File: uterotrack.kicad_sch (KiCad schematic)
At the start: 77 parts, among them J1 RFShield, J2 MicroSD_Card, J3 Argos_Prog, J4 AS5510, J5 Prog, J6 EXP, Q1 DMP2110UW, Q10 MMBT2222, Q11 MMBT2222, Q12 MMBT2222, Q13 MMBT2222, Q2 DMP2110UW, Q3 MMBT2222, Q4 DMP2110UW, Q5 DMP2110UW, Q6 MMBT2222, Q7 SiS415DNT, Q8 DMP2110UW, Q9 MMBT2222, U1 Argos_SMD, U2 ESP32-S3-WROOM-1, U3 keller_6LHPD, U4 RV-3032-C7, U5 CAM-M8Q

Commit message: Change manf# and footprint of resistor of 4k7, 20k and 100k to 0402
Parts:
- J3: manf# (none) -> 53047-0510
- R15, R16, R17, R23, R24, R26, R27, R28, R30, R31, R32, R33, R34, R36, R37: footprint Resistor_SMD:R_0603_1608Metric -> Resistor_SMD:R_0402_1005Metric; manf# CRCW0603100KFKEAC -> CRCW0402100KFKEDC
- R19, R20, R21, R22, R25: footprint Resistor_SMD:R_0603_1608Metric -> Resistor_SMD:R_0402_1005Metric; manf# CRCW06034K70FKEAC -> CRCW04024K70FKEDC
- R29, R35: footprint Resistor_SMD:R_0603_1608Metric -> Resistor_SMD:R_0402_1005Metric; manf# CRCW060320K0FKEAC -> CRCW040220K0FKEDC
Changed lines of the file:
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@@
 			)
 		)
-		(property "Footprint" "Resistor_SMD:R_0603_1608Metric"
+		(property "Footprint" "Resistor_SMD:R_0402_1005Metric"
 			(at 64.77 248.158 90)
 			(effects
@@
 			)
 		)
-		(property "manf#" "CRCW0603100KFKEAC"
+		(property "manf#" "CRCW0402100KFKEDC"
 			(at 64.77 246.38 0)
 			(effects
@@
 			)
 		)
-		(property "Footprint" "Resistor_SMD:R_0603_1608Metric"
+		(property "Footprint" "Resistor_SMD:R_0402_1005Metric"
 			(at 87.63 169.418 90)
 			(effects
@@
 			)
 		)
-		(property "manf#" "CRCW0603100KFKEAC"
+		(property "manf#" "CRCW0402100KFKEDC"
 			(at 87.63 167.64 0)
 			(effects
@@
 			)
 		)
-		(property "Footprint" "Resistor_SMD:R_0603_1608Metric"
+		(property "Footprint" "Resistor_SMD:R_0402_1005Metric"
 			(at 82.042 156.21 90)
 			(effects
@@
 			)
 		)
-		(property "manf#" "CRCW0603100KFKEAC"
+		(property "manf#" "CRCW0402100KFKEDC"
 			(at 83.82 156.21 0)
 			(effects
@@
 			)
 		)
-		(property "Footprint" "Resistor_SMD:R_0603_1608Metric"
+		(property "Footprint" "Resistor_SMD:R_0402_1005Metric"
 			(at 120.142 234.95 90)
 			(effects
@@
 			)
 		)
-		(property "manf#" "CRCW0603100KFKEAC"
+		(property "manf#" "CRCW0402100KFKEDC"
 			(at 121.92 234.95 0)
 			(effects
@@
 			)
 		)
-		(property "Footprint" "Resistor_SMD:R_0603_1608Metric"
+		(property "Footprint" "Resistor_SMD:R_0402_1005Metric"
 			(at 62.23 155.702 90)
 			(effects
@@
 			)
 		)
-		(property "manf#" "CRCW06034K70FKEAC"
+		(property "manf#" "CRCW04024K70FKEDC"
 			(at 62.23 157.48 0)
 			(effects
@@
 			)
 		)
-		(property "Footprint" "Resistor_SMD:R_0603_1608Metric"
+		(property "Footprint" "Resistor_SMD:R_0402_1005Metric"
 			(at 108.458 247.65 90)
 			(effects
@@
 			)
 		)
-		(property "manf#" "CRCW060320K0FKEAC"
+		(property "manf#" "CRCW040220K0FKEDC"
 			(at 106.68 247.65 0)
 			(effects
@@
 			)
 		)
-		(property "Footprint" "Resistor_SMD:R_0603_1608Metric"
+		(property "Footprint" "Resistor_SMD:R_0402_1005Metric"
 			(at 92.202 173.99 90)
 			(effects
@@
 			)
 		)
-		(property "manf#" "CRCW0603100KFKEAC"
+		(property "manf#" "CRCW0402100KFKEDC"
 			(at 93.98 173.99 0)
 			(effects
@@
 			)
 		)
-		(property "Footprint" "Resistor_SMD:R_0603_1608Metric"
+		(property "Footprint" "Resistor_SMD:R_0402_1005Metric"
 			(at 62.23 156.718 90)
 			(effects
@@
 			)
 		)
-		(property "manf#" "CRCW06034K70FKEAC"
+		(property "manf#" "CRCW04024K70FKEDC"
 			(at 62.23 154.94 0)
 			(effects
@@
 			)
 		)
-		(property "Footprint" "Resistor_SMD:R_0603_1608Metric"
+		(property "Footprint" "Resistor_SMD:R_0402_1005Metric"
 			(at 59.182 234.95 90)
 			(effects
@@
 			)
 		)
-		(property "manf#" "CRCW0603100KFKEAC"
+		(property "manf#" "CRCW0402100KFKEDC"
 			(at 60.96 234.95 0)
 			(effects
@@
 			)
 		)
-		(property "Footprint" "Resistor_SMD:R_0603_1608Metric"
+		(property "Footprint" "Resistor_SMD:R_0402_1005Metric"
 			(at 196.85 260.858 90)
 			(effects
@@
 			)
 		)
-		(property "manf#" "CRCW0603100KFKEAC"
+		(property "manf#" "CRCW0402100KFKEDC"
 			(at 196.85 259.08 0)
 			(effects
@@
 			)
 		)
-		(property "Footprint" "Resistor_SMD:R_0603_1608Metric"
+		(property "Footprint" "Resistor_SMD:R_0402_1005Metric"
 			(at 125.73 248.158 90)
 			(effects
@@
 			)
 		)
-		(property "manf#" "CRCW0603100KFKEAC"
+		(property "manf#" "CRCW0402100KFKEDC"
 			(at 125.73 246.38 0)
 			(effects
@@
 			)
 		)
-		(property "Footprint" "Resistor_SMD:R_0603_1608Metric"
+		(property "Footprint" "Resistor_SMD:R_0402_1005Metric"
 			(at 290.83 85.598 90)
 			(effects
@@
 			)
 		)
-		(property "manf#" "CRCW0603100KFKEAC"
+		(property "manf#" "CRCW0402100KFKEDC"
 			(at 290.83 83.82 0)
 			(effects
@@
 			)
 		)
-		(property "Footprint" "Resistor_SMD:R_0603_1608Metric"
+		(property "Footprint" "Resistor_SMD:R_0402_1005Metric"
 			(at 105.41 113.538 90)
 			(effects
@@
 			)
 		)
-		(property "manf#" "CRCW06034K70FKEAC"
+		(property "manf#" "CRCW04024K70FKEDC"
 			(at 105.41 111.76 0)
 			(effects
@@
 			)
 		)
+		(property "manf#" "53047-0510"
+			(at 287.02 114.3 0)
+			(effects
+				(font
+					(size 1.27 1.27)
+				)
+				(hide yes)
+			)
+		)
 		(pin "2"
 		)
@@
 			)
 		)
-		(property "Footprint" "Resistor_SMD:R_0603_1608Metric"
+		(property "Footprint" "Resistor_SMD:R_0402_1005Metric"
 			(at 296.418 72.39 90)
 			(effects
@@
 			)
 		)
-		(property "manf#" "CRCW0603100KFKEAC"
+		(property "manf#" "CRCW0402100KFKEDC"
 			(at 294.64 72.39 0)
 			(effects
@@
 			)
 		)
-		(property "Footprint" "Resistor_SMD:R_0603_1608Metric"
+		(property "Footprint" "Resistor_SMD:R_0402_1005Metric"
 			(at 127.762 156.21 90)
 			(effects
@@
 			)
 		)
-		(property "manf#" "CRCW0603100KFKEAC"
+		(property "manf#" "CRCW0402100KFKEDC"
 			(at 129.54 156.21 0)
 			(effects
@@
 			)
 		)
-		(property "Footprint" "Resistor_SMD:R_0603_1608Metric"
+		(property "Footprint" "Resistor_SMD:R_0402_1005Metric"
 			(at 46.482 74.93 90)
 			(effects
@@
 			)
 		)
-		(property "manf#" "CRCW0603100KFKEAC"
+		(property "manf#" "CRCW0402100KFKEDC"
 			(at 48.26 74.93 0)
 			(effects
@@
 			)
 		)
-		(property "Footprint" "Resistor_SMD:R_0603_1608Metric"
+		(property "Footprint" "Resistor_SMD:R_0402_1005Metric"
 			(at 69.342 252.73 90)
 			(effects
@@
 			)
 		)
-		(property "manf#" "CRCW0603100KFKEAC"
+		(property "manf#" "CRCW0402100KFKEDC"
 			(at 71.12 252.73 0)
 			(effects
@@
 			)
 		)
-		(property "Footprint" "Resistor_SMD:R_0603_1608Metric"
+		(property "Footprint" "Resistor_SMD:R_0402_1005Metric"
 			(at 49.53 109.982 90)
 			(effects
@@
 			)
 		)
-		(property "manf#" "CRCW06034K70FKEAC"
+		(property "manf#" "CRCW04024K70FKEDC"
 			(at 49.53 111.76 0)
 			(effects
@@
 			)
 		)
-		(property "Footprint" "Resistor_SMD:R_0603_1608Metric"
+		(property "Footprint" "Resistor_SMD:R_0402_1005Metric"
 			(at 201.93 245.618 90)
 			(effects
@@
 			)
 		)
-		(property "manf#" "CRCW0603100KFKEAC"
+		(property "manf#" "CRCW0402100KFKEDC"
 			(at 201.93 243.84 0)
 			(effects
@@
 			)
 		)
-		(property "Footprint" "Resistor_SMD:R_0603_1608Metric"
+		(property "Footprint" "Resistor_SMD:R_0402_1005Metric"
 			(at 108.458 234.95 90)
 			(effects
@@
 			)
 		)
-		(property "manf#" "CRCW060320K0FKEAC"
+		(property "manf#" "CRCW040220K0FKEDC"
 			(at 106.68 234.95 0)
 			(effects
@@
 			)
 		)
-		(property "Footprint" "Resistor_SMD:R_0603_1608Metric"
+		(property "Footprint" "Resistor_SMD:R_0402_1005Metric"
 			(at 49.53 110.998 90)
 			(effects
@@
 			)
 		)
-		(property "manf#" "CRCW06034K70FKEAC"
+		(property "manf#" "CRCW04024K70FKEDC"
 			(at 49.53 109.22 0)
 			(effects
@@
 			)
 		)
-		(property "Footprint" "Resistor_SMD:R_0603_1608Metric"
+		(property "Footprint" "Resistor_SMD:R_0402_1005Metric"
 			(at 161.29 245.618 90)
 			(effects
@@
 			)
 		)
-		(property "manf#" "CRCW0603100KFKEAC"
+		(property "manf#" "CRCW0402100KFKEDC"
 			(at 161.29 243.84 0)
 			(effects

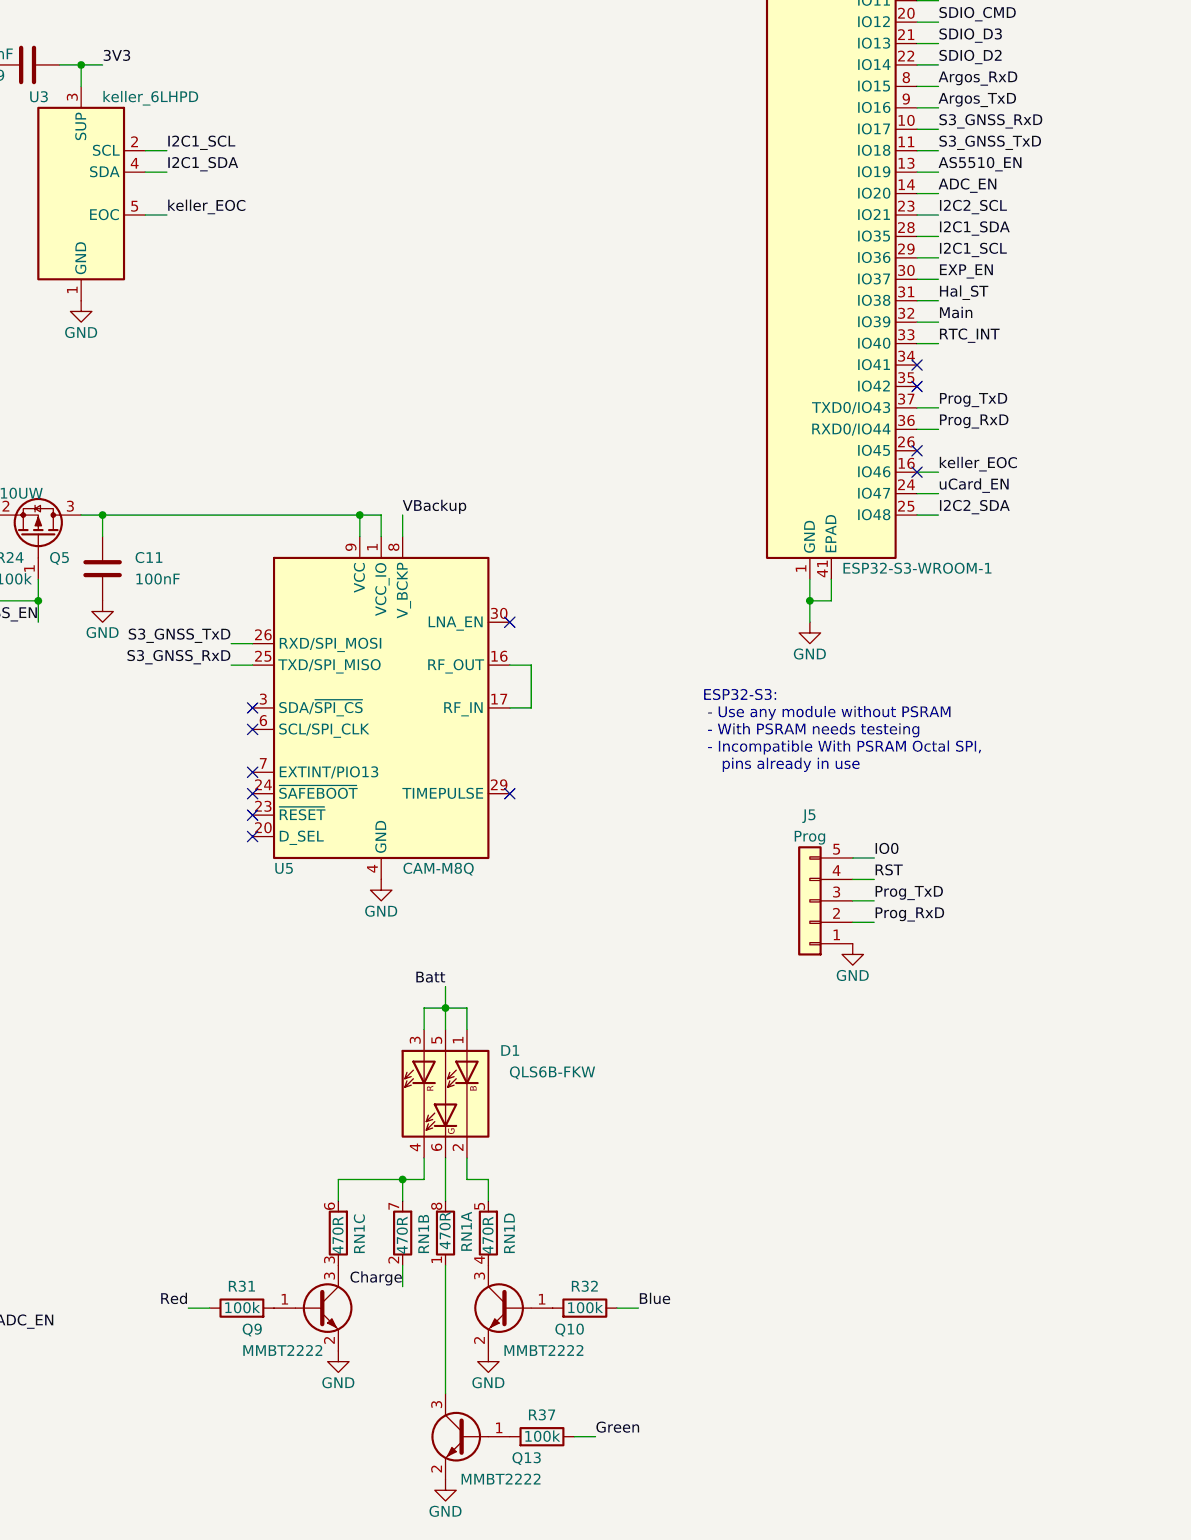
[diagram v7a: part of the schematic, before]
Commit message: Move AS5510_EN to IO42 and switch led red with charge in RN1
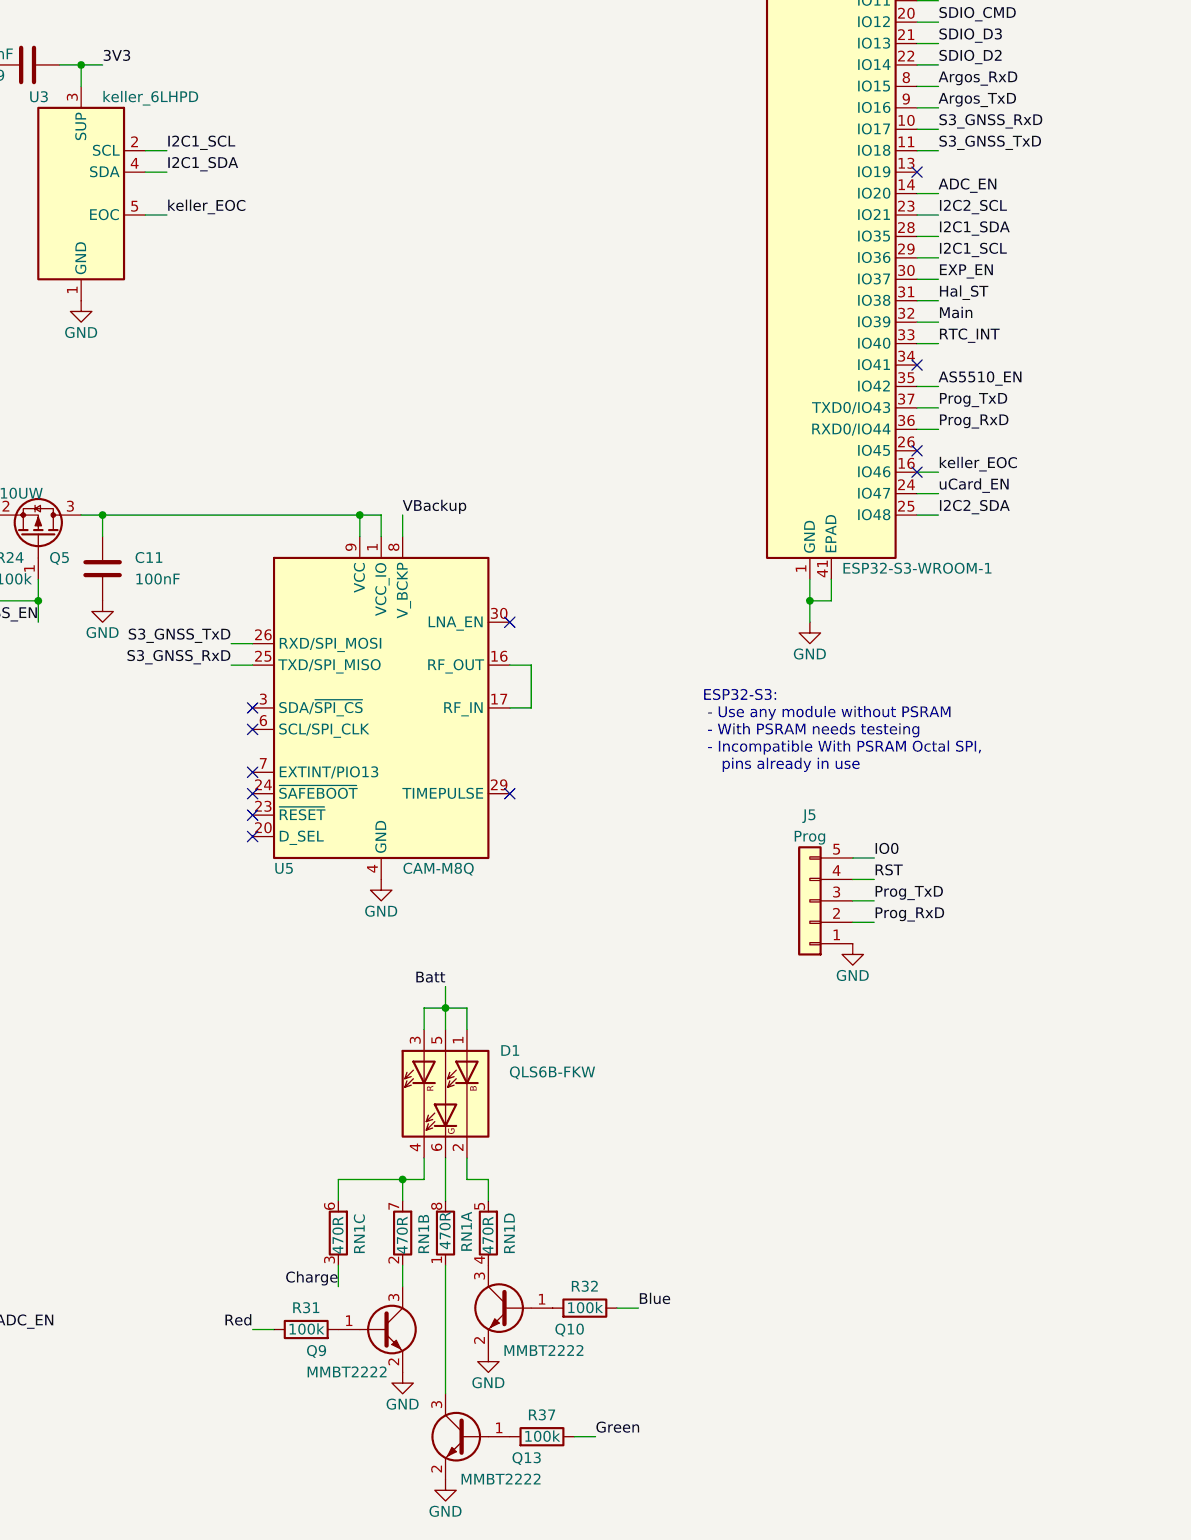
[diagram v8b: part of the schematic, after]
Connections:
- net AS5510_EN: now also U2.35 (IO42); no longer U2.13 (IO19)
- net Charge: now also RN1.3 (R3.1); no longer RN1.2 (R2.1)
- net at Q9.3 (C): now also RN1.2 (R2.1); no longer RN1.3 (R3.1)
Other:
- moved on the sheet: Q9, R31
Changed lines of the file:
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@@
 	)
 	(no_connect
-		(at 241.3 134.62)
+		(at 241.3 109.22)
 	)
 	(no_connect
@@
 	(wire
 		(pts
+			(xy 180.34 238.76) (xy 180.34 241.3)
+		)
+		(stroke
+			(width 0)
+			(type default)
+		)
+	)
+	(wire
+		(pts
 			(xy 358.14 86.36) (xy 355.6 86.36)
 		)
@@
 	(wire
 		(pts
-			(xy 157.48 243.84) (xy 154.94 243.84)
+			(xy 165.1 246.38) (xy 162.56 246.38)
 		)
 		(stroke
@@
 	(wire
 		(pts
-			(xy 243.84 109.22) (xy 241.3 109.22)
+			(xy 243.84 134.62) (xy 241.3 134.62)
 		)
 		(stroke
@@
 	(wire
 		(pts
-			(xy 180.34 238.76) (xy 180.34 241.3)
+			(xy 172.72 238.76) (xy 172.72 241.3)
 		)
 		(stroke
@@
 	)
 	(label "Charge"
-		(at 180.34 241.3 180)
+		(at 172.72 241.3 180)
 		(effects
 			(font
@@
 	)
 	(label "AS5510_EN"
-		(at 243.84 109.22 0)
+		(at 243.84 134.62 0)
 		(effects
 			(font
@@
 	)
 	(label "Red"
-		(at 154.94 243.84 180)
+		(at 162.56 246.38 180)
 		(effects
 			(font
@@
 	(symbol
 		(lib_id "Transistor_BJT:Q_NPN_BEC")
-		(at 170.18 243.84 0)
+		(at 177.8 246.38 0)
 		(unit 1)
 		(exclude_from_sim no)
@@
 		(dnp no)
 		(property "Reference" "Q9"
-			(at 161.29 246.38 0)
+			(at 168.91 248.92 0)
 			(effects
 				(font
@@
 		)
 		(property "Value" "MMBT2222"
-			(at 161.29 248.92 0)
+			(at 168.91 251.46 0)
 			(effects
 				(font
@@
 		)
 		(property "Footprint" "Package_TO_SOT_SMD:SOT-323_SC-70"
-			(at 175.26 241.3 0)
+			(at 182.88 243.84 0)
 			(effects
 				(font
@@
 		)
 		(property "Datasheet" "~"
-			(at 170.18 243.84 0)
+			(at 177.8 246.38 0)
 			(effects
 				(font
@@
 		)
 		(property "Description" "NPN transistor, base/emitter/collector"
-			(at 170.18 243.84 0)
+			(at 177.8 246.38 0)
 			(effects
 				(font
@@
 		)
 		(property "manf#" "MMBT2222AWT3G"
-			(at 170.18 243.84 0)
+			(at 177.8 246.38 0)
 			(effects
 				(font
@@
 	(symbol
 		(lib_id "power:GND")
-		(at 172.72 248.92 0)
+		(at 180.34 251.46 0)
 		(unit 1)
 		(exclude_from_sim no)
@@
 		(dnp no)
 		(property "Reference" "#PWR026"
-			(at 172.72 255.27 0)
+			(at 180.34 257.81 0)
 			(effects
 				(font
@@
 		)
 		(property "Value" "GND"
-			(at 172.72 252.73 0)
+			(at 180.34 255.27 0)
 			(effects
 				(font
@@
 		)
 		(property "Footprint" ""
-			(at 172.72 248.92 0)
+			(at 180.34 251.46 0)
 			(effects
 				(font
@@
 		)
 		(property "Datasheet" ""
-			(at 172.72 248.92 0)
+			(at 180.34 251.46 0)
 			(effects
 				(font
@@
 		)
 		(property "Description" ""
-			(at 172.72 248.92 0)
+			(at 180.34 251.46 0)
 			(effects
 				(font
@@
 	(symbol
 		(lib_id "Device:R")
-		(at 161.29 243.84 90)
+		(at 168.91 246.38 90)
 		(unit 1)
 		(exclude_from_sim no)
@@
 		(dnp no)
 		(property "Reference" "R31"
-			(at 161.29 241.3 90)
+			(at 168.91 243.84 90)
 			(effects
 				(font
@@
 		)
 		(property "Value" "100k"
-			(at 161.29 243.84 90)
+			(at 168.91 246.38 90)
 			(effects
 				(font
@@
 		)
 		(property "Footprint" "Resistor_SMD:R_0402_1005Metric"
-			(at 161.29 245.618 90)
+			(at 168.91 248.158 90)
 			(effects
 				(font
@@
 		)
 		(property "Datasheet" "~"
-			(at 161.29 243.84 0)
+			(at 168.91 246.38 0)
 			(effects
 				(font
@@
 		)
 		(property "Description" "Resistor"
-			(at 161.29 243.84 0)
+			(at 168.91 246.38 0)
 			(effects
 				(font
@@
 		)
 		(property "manf#" "CRCW0402100KFKEDC"
-			(at 161.29 243.84 0)
+			(at 168.91 246.38 0)
 			(effects
 				(font
